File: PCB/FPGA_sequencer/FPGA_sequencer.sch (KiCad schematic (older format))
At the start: 57 parts, among them J1 Conn_Coaxial, U1 ADA4940-2ACPZ-R7_a, U2 AD9648BCPZ-125, U3 DB3S406F0L, U4 DB3S406F0L, U5 AD8065ARTZ-R2, U6 MAX4564EKA+T

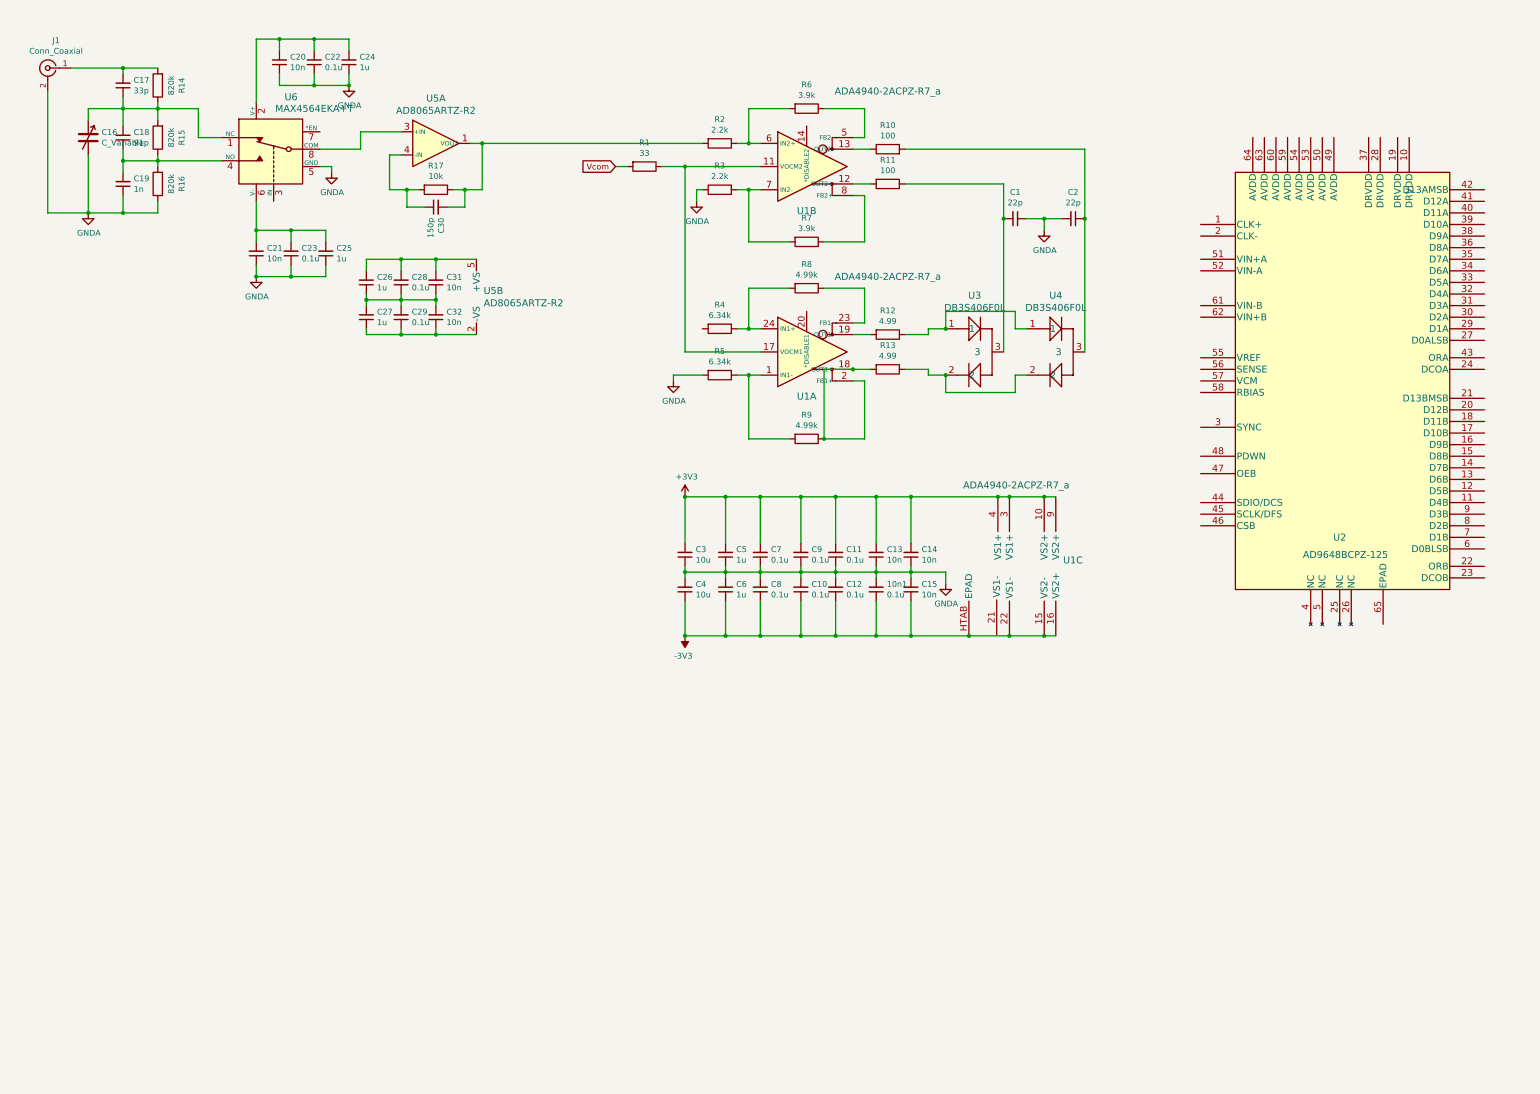
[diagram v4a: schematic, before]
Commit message: Current Controller and GradientDriver_rev2
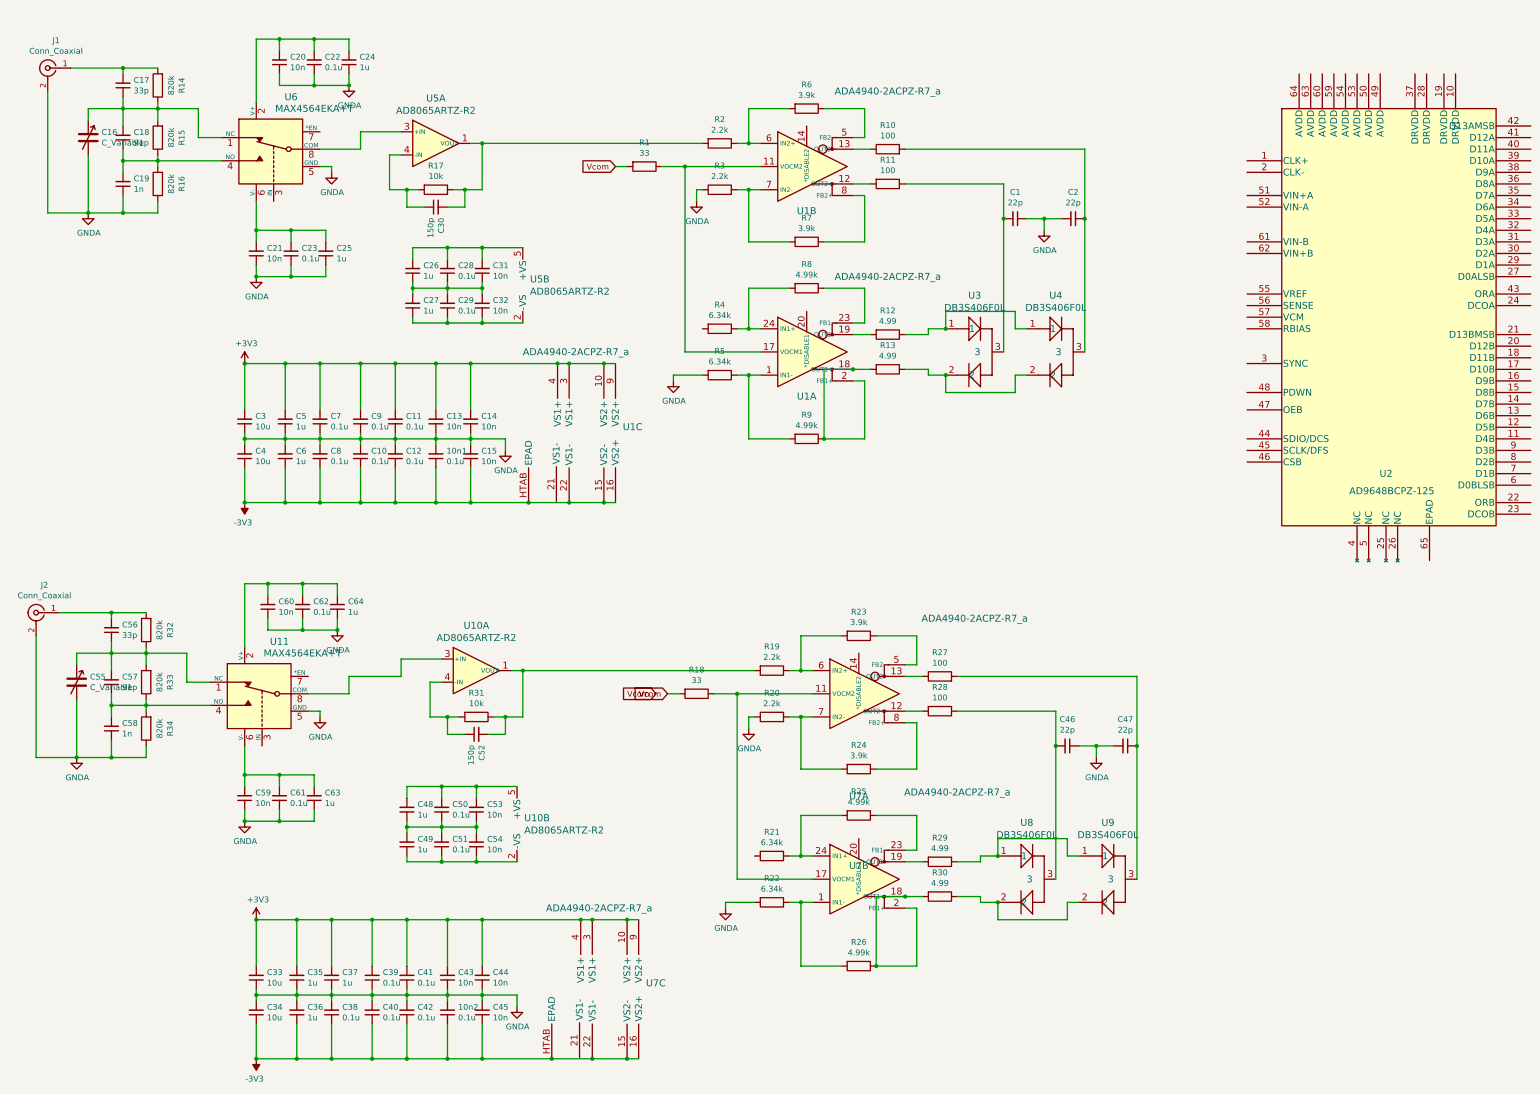
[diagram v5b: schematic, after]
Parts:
- added 10n2, C38, C39, C40, C41, C42, C50, C51, C61, C62: 0.1u, Capacitor_SMD:C_0402_1005Metric, symbol Device:C_Small
- added C33, C34: 10u, Capacitor_SMD:C_0402_1005Metric, symbol Device:C_Small
- added C35, C36, C37, C48, C49, C63, C64: 1u, Capacitor_SMD:C_0402_1005Metric, symbol Device:C_Small
- added C43, C44, C45, C53, C54, C59, C60: 10n, Capacitor_SMD:C_0402_1005Metric, symbol Device:C_Small
- added C46, C47: 22p, Capacitor_SMD:C_0402_1005Metric, symbol Device:C_Small
- added C52: 150p, Capacitor_SMD:C_0402_1005Metric, symbol Device:C_Small
- added C55: C_Variable, Capacitor_SMD:C_Trimmer_Murata_TZB4-A, symbol Device:C_Variable
- added C56: 33p, Capacitor_SMD:C_0402_1005Metric, symbol Device:C_Small
- added C57: 91p, Capacitor_SMD:C_0402_1005Metric, symbol Device:C_Small
- added C58: 1n, Capacitor_SMD:C_0402_1005Metric, symbol Device:C_Small
- added J2: Conn_Coaxial, Connector_Coaxial:SMA_Amphenol_132134-11_Vertical, symbol Connector:Conn_Coaxial
- added R18: 33, Resistor_SMD:R_0402_1005Metric, symbol Device:R
- added R19, R20: 2.2k, Resistor_SMD:R_0402_1005Metric, symbol Device:R
- added R21, R22: 6.34k, Resistor_SMD:R_0402_1005Metric, symbol Device:R
- added R23, R24: 3.9k, Resistor_SMD:R_0402_1005Metric, symbol Device:R
- added R25, R26: 4.99k, Resistor_SMD:R_0402_1005Metric, symbol Device:R
- added R27, R28: 100, Resistor_SMD:R_0402_1005Metric, symbol Device:R
- added R29, R30: 4.99, Resistor_SMD:R_0402_1005Metric, symbol Device:R
- added R31: 10k, Resistor_SMD:R_0402_1005Metric, symbol Device:R
- added R32, R33, R34: 820k, Resistor_SMD:R_0402_1005Metric, symbol Device:R
- added U10: AD8065ARTZ-R2, FPGA_sequencer:AD8065ARTZ-R2, symbol FPGA_sequencer:AD8065ARTZ-R2
- added U11: MAX4564EKA+T, FPGA_sequencer:MAX4564EKA&plus_T, symbol FPGA_sequencer:MAX4564EKA+T
- added U7: ADA4940-2ACPZ-R7_a, FPGA_sequencer:ADA4940-2ACPZ-R7, symbol FPGA_sequencer:ADA4940-2ACPZ-R7_a
- added U8, U9: DB3S406F0L, FPGA_sequencer:DB3S406F0L, symbol FPGA_sequencer:DB3S406F0L
- 10n1, C1, C10, C11, C12, C13, C14, C15, C17, C18, C19, C2, C20, C21, C22, C23, C24, C25, C26, C27, C28, C29, C3, C30, C31, C32, C4, C5, C6, C7, C8, C9: footprint Capacitor_SMD:C_0603_1608Metric -> Capacitor_SMD:C_0402_1005Metric
- R1, R10, R11, R12, R13, R14, R15, R16, R17, R2, R3, R4, R5, R6, R7, R8, R9: footprint Resistor_SMD:R_0603_1608Metric -> Resistor_SMD:R_0402_1005Metric
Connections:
- net +3V3: now also C33.2, C35.2, C37.2, C39.2, C41.2, C43.2, C44.2, U7.10 (VS2+), U7.3 (VS1+), U7.4 (VS1+), U7.9 (VS2+)
- net -3V3: now also 10n2.1, C34.1, C36.1, C38.1, C40.1, C42.1, C45.1, U7.15 (VS2-), U7.16 (VS2+), U7.22 (VS1-), U7.HTAB (EPAD)
- net GNDA: now also 10n2.2, C33.1, C34.2, C35.1, C36.2, C37.1, C38.2, C39.1, C40.2, C41.1, C42.2, C43.1, C44.1, C45.2, C46.1, C47.2, C55.2, C58.1, C59.1, C60.1, C61.1, C62.1, C63.1, C64.1, J2.2 (Ext), R20.1, R22.2, R34.1, U11.5 (GND)
- net Vcom: now also R18.2
- new net: R18.1, U7.11 (VOCM2), U7.17 (VOCM1)
- new net: R28.2, U7.12 (OUT2+)
- new net: R27.1, U7.13 (OUT2-)
- new net: R23.1, U7.5 (FB2-)
- new net: R19.1, R23.2, U7.6 (IN2+)
- new net: R20.2, R24.2, U7.7 (IN2-)
- new net: R24.1, U7.8 (FB2+)
- new net: R22.1, R26.2, U7.1 (IN1-)
- new net: R26.1, R30.2, U7.18 (OUT1+), U7.2 (FB1+)
- new net: R29.2, U7.19 (OUT1-)
- new net: R25.1, U7.23 (FB1-)
- new net: R21.1, R25.2, U7.24 (IN1+)
- new net: R29.1, U8.1, U9.1
- new net: R30.1, U8.2, U9.2
- new net: C46.2, R28.1, U8.3
- new net: C47.1, R27.2, U9.3
- new net: C52.2, R19.2, R31.1, U10.1 (VOUT)
- new net: U10.3 (+IN), U11.8 (COM)
- new net: C52.1, R31.2, U10.4 (-IN)
- new net: C49.1, C51.1, C54.1, U10.2 (-VS)
- new net: C48.2, C50.2, C53.2, U10.5 (+VS)
- new net: C48.1, C49.2, C50.1, C51.2, C53.1, C54.2
- new net: C55.1, C56.1, C57.2, R32.1, R33.2, U11.1 (NC)
- new net: C60.2, C62.2, C64.2, U11.2 (V+)
- new net: C57.1, C58.2, R33.1, R34.2, U11.4 (NO)
- new net: C59.2, C61.2, C63.2, U11.6 (V-)
- new net: C56.2, J2.1 (In), R32.2
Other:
- moved on the sheet: 10n1, C10, C11, C12, C13, C14, C15, C26, C27, C28, C29, C3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
